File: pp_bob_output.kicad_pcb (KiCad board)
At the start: 2 copper layers, 98.8 x 72.1 mm, 38 parts, among them P4 13X2, U1 74LS540, U2 74LVC245, U3 74LS541

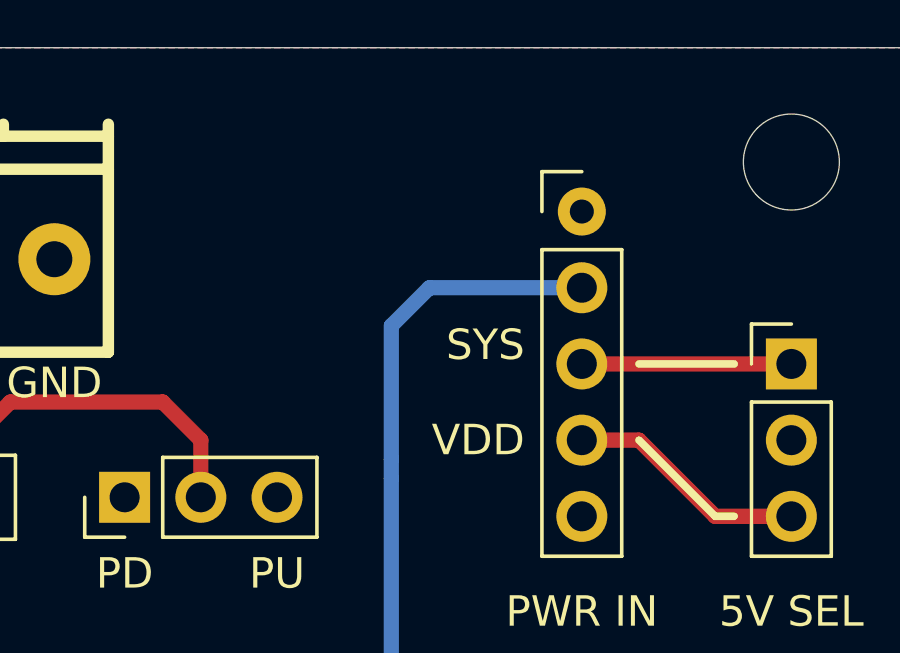
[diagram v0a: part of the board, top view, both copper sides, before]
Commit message: Fix silkscreen to top
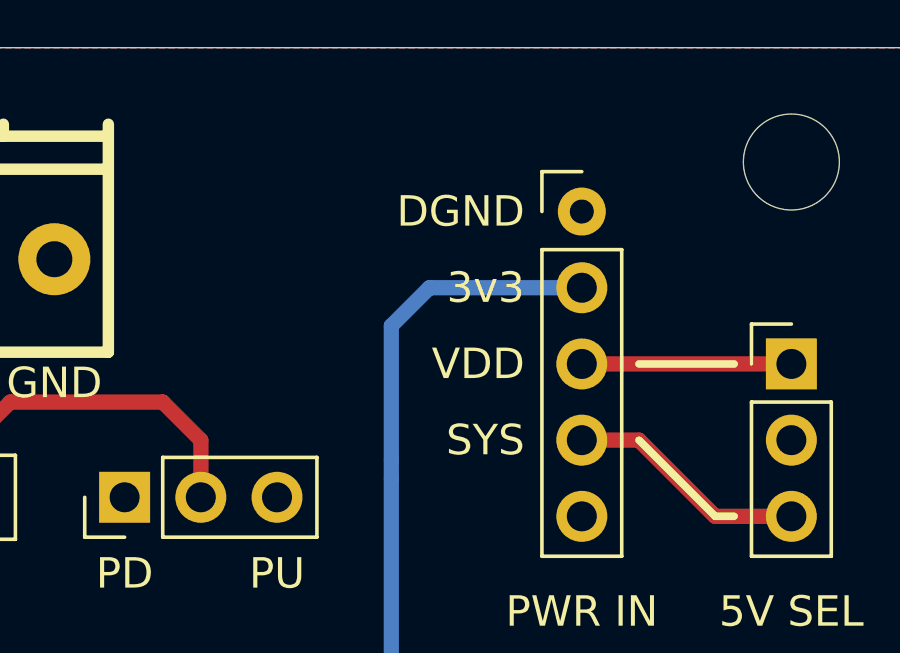
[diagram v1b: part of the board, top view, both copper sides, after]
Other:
- board text added: "3v3"
- board text added: "DGND"
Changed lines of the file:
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@@
-(kicad_pcb (version 20170123) (host pcbnew no-vcs-found-ecdfa40~58~ubuntu16.04.1)
+(kicad_pcb (version 4) (host pcbnew 4.0.7-e2-6376~58~ubuntu16.04.1)
   (general
     (links 129)
     (no_connects 0)
-    (area 25.095 24.0525 124.432905 99.0185)
+    (area 25.387299 25.387299 124.218701 97.548701)
     (thickness 1.6)
-    (drawings 75)
+    (drawings 77)
     (tracks 360)
     (zones 0)
@@
   (page A4)
   (layers
-    (0 F.Cu signal)
-    (31 B.Cu signal)
+    (0 F.Cu signal hide)
+    (31 B.Cu signal hide)
     (32 B.Adhes user)
     (33 F.Adhes user)
@@
       (hpglpenspeed 20)
       (hpglpendiameter 15)
+      (hpglpenoverlay 2)
       (psnegative false)
       (psa4output false)
@@
     (descr "20-lead dip package, row spacing 7.62 mm (300 mils), LongPads")
     (tags "DIL DIP PDIP 2.54mm 7.62mm 300mil LongPads")
-    (fp_text reference U1 (at 3.81 -2.39 90) (layer F.SilkS)
+    (fp_text reference U1 (at 3.81 -2.39 450) (layer F.SilkS)
       (effects (font (size 1 1) (thickness 0.15)))
     )
@@
     )
   )
+  (gr_text 3v3 (at 111.506 33.401) (layer F.SilkS)
+    (effects (font (size 1.016 1.016) (thickness 0.2032)) (justify right))
+  )
+  (gr_text DGND (at 111.506 30.861) (layer F.SilkS)
+    (effects (font (size 1.016 1.016) (thickness 0.2032)) (justify right))
+  )
   (gr_line (start 117.856 41.021) (end 115.316 38.481) (angle 90) (layer F.SilkS) (width 0.254))
   (gr_line (start 118.491 41.021) (end 117.856 41.021) (angle 90) (layer F.SilkS) (width 0.254))
@@
     (effects (font (size 1.016 1.016) (thickness 0.2032)))
   )
-  (gr_text VDD (at 111.506 38.481) (layer F.SilkS)
+  (gr_text SYS (at 111.506 38.481) (layer F.SilkS)
     (effects (font (size 1.016 1.016) (thickness 0.2032)) (justify right))
   )
-  (gr_text SYS (at 111.506 35.306) (layer F.SilkS)
+  (gr_text VDD (at 111.506 35.941) (layer F.SilkS)
     (effects (font (size 1.016 1.016) (thickness 0.2032)) (justify right))
   )
